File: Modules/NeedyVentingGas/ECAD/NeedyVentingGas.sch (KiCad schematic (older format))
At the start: 15 parts, among them J1 comm_header, J2 prog_header, SW1 Y_Switch, SW2 N_Switch, U1 ATmega328-PU, U2 MAX7219, U3 LTD6640E

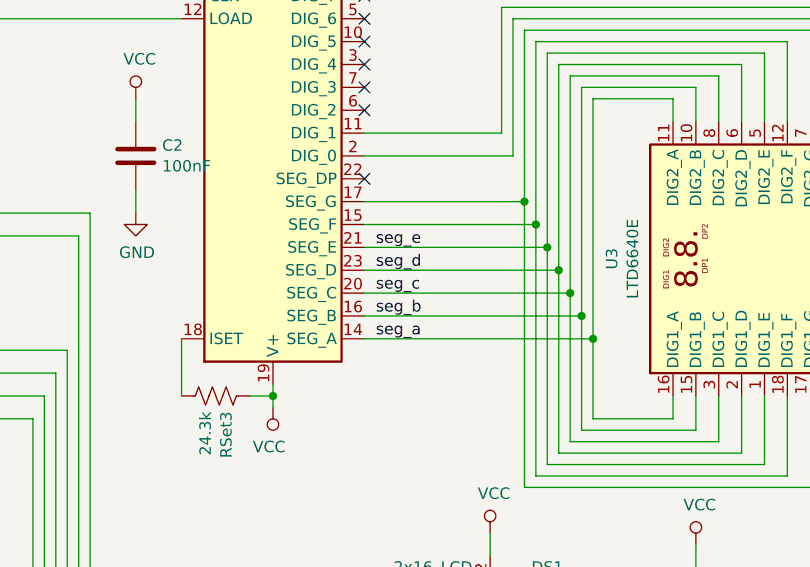
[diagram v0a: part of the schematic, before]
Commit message: Removed unused labels
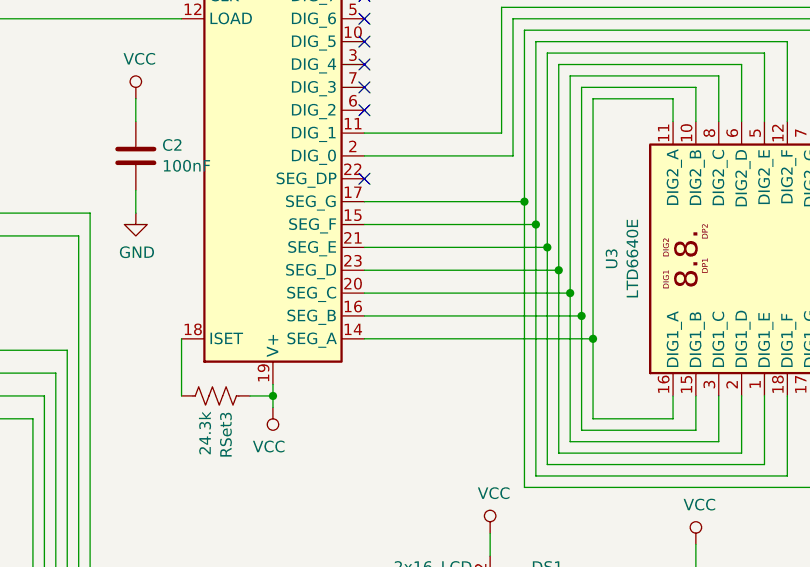
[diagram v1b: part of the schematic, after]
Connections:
- net seg_a: no longer names the net of U2.14 (SEG_A), U3.11 (DIG2_A), U3.16 (DIG1_A)
- net seg_b: no longer names the net of U2.16 (SEG_B), U3.10 (DIG2_B), U3.15 (DIG1_B)
- net seg_c: no longer names the net of U2.20 (SEG_C), U3.3 (DIG1_C), U3.8 (DIG2_C)
- net seg_d: no longer names the net of U2.23 (SEG_D), U3.2 (DIG1_D), U3.6 (DIG2_D)
- net seg_e: no longer names the net of U2.21 (SEG_E), U3.1 (DIG1_E), U3.5 (DIG2_E)
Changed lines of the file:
@@
 EESchema Schematic File Version 4
-LIBS:VentingGas-cache
+LIBS:NeedyVentingGas-cache
 EELAYER 29 0
 EELAYER END
@@
 Wire Wire Line
 	7000 2300 7000 3050
-Text Label 6350 3250 0    50   ~ 0
-seg_e
-Text Label 6350 3350 0    50   ~ 0
-seg_d
-Text Label 6350 3450 0    50   ~ 0
-seg_c
-Text Label 6350 3550 0    50   ~ 0
-seg_b
-Text Label 6350 3650 0    50   ~ 0
-seg_a
 Wire Wire Line
 	6300 3050 7000 3050

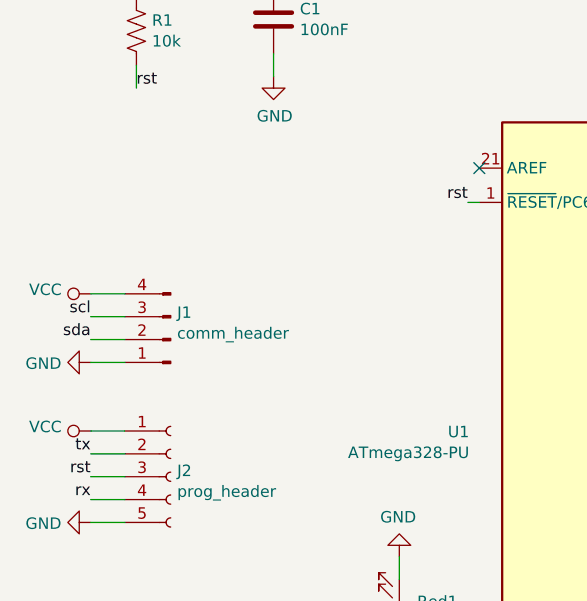
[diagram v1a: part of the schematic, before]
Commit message: Added polyfuses to all modules
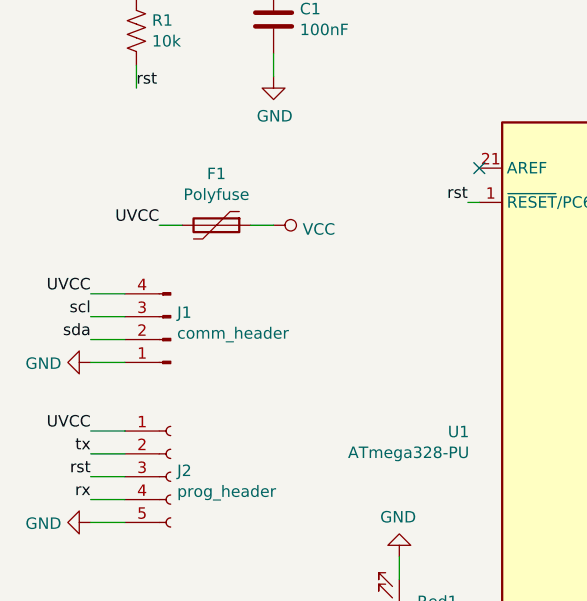
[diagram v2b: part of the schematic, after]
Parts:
- added F1: Polyfuse, symbol Device:Polyfuse
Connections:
- net VCC: now also F1.1; no longer J1.4 (Pin_4), J2.1 (Pin_1)
- new net UVCC: F1.2, J1.4 (Pin_4), J2.1 (Pin_1)
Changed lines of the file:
@@
 L power:VCC #PWR01
 U 1 1 5F5DC5B2
-P 1400 3350
-F 0 "#PWR01" H 1400 3200 50  0001 C CNN
-F 1 "VCC" V 1418 3477 50  0000 L CNN
-F 2 "" H 1400 3350 50  0001 C CNN
-F 3 "" H 1400 3350 50  0001 C CNN
-	1    1400 3350
-	0    -1   -1   0
-$EndComp
-$Comp
-L power:VCC #PWR03
-U 1 1 5F5DD568
-P 1400 3950
-F 0 "#PWR03" H 1400 3800 50  0001 C CNN
-F 1 "VCC" V 1418 4077 50  0000 L CNN
-F 2 "" H 1400 3950 50  0001 C CNN
-F 3 "" H 1400 3950 50  0001 C CNN
-	1    1400 3950
-	0    -1   -1   0
+P 2200 3050
+F 0 "#PWR01" H 2200 2900 50  0001 C CNN
+F 1 "VCC" V 2218 3177 50  0000 L CNN
+F 2 "" H 2200 3050 50  0001 C CNN
+F 3 "" H 2200 3050 50  0001 C CNN
+	1    2200 3050
+	0    1    1    0
 $EndComp
 $Comp
@@
 Wire Wire Line
 	5200 6450 5350 6450
+$Comp
+L Device:Polyfuse F1
+U 1 1 5F92430F
+P 1950 3050
+F 0 "F1" V 1725 3050 50  0000 C CNN
+F 1 "Polyfuse" V 1816 3050 50  0000 C CNN
+F 2 "" H 2000 2850 50  0001 L CNN
+F 3 "~" H 1950 3050 50  0001 C CNN
+	1    1950 3050
+	0    1    1    0
+$EndComp
+Text Label 1400 3350 2    50   ~ 0
+UVCC
+Text Label 1400 3950 2    50   ~ 0
+UVCC
+Text Label 1700 3050 2    50   ~ 0
+UVCC
+Wire Wire Line
+	1700 3050 1800 3050
+Wire Wire Line
+	2100 3050 2200 3050
 $EndSCHEMATC
